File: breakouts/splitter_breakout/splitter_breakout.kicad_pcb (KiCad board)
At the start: 4 copper layers, 29.5 x 23.4 mm, 4 parts, among them U101 CONN_SMA_2GND, U102 CONN_SMA_2GND, U103 CONN_SMA_2GND, U3 PWR_SPLITTER

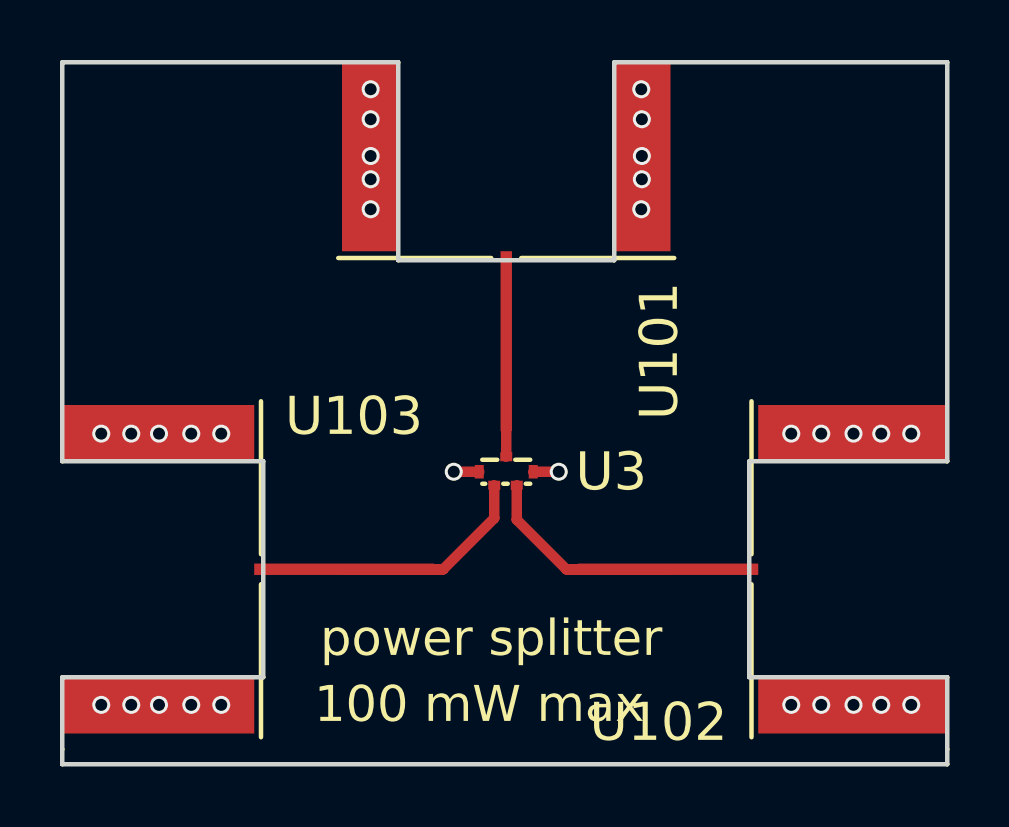
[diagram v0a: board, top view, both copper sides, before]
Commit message: modified splitter breakout to use coplanar waveguide.
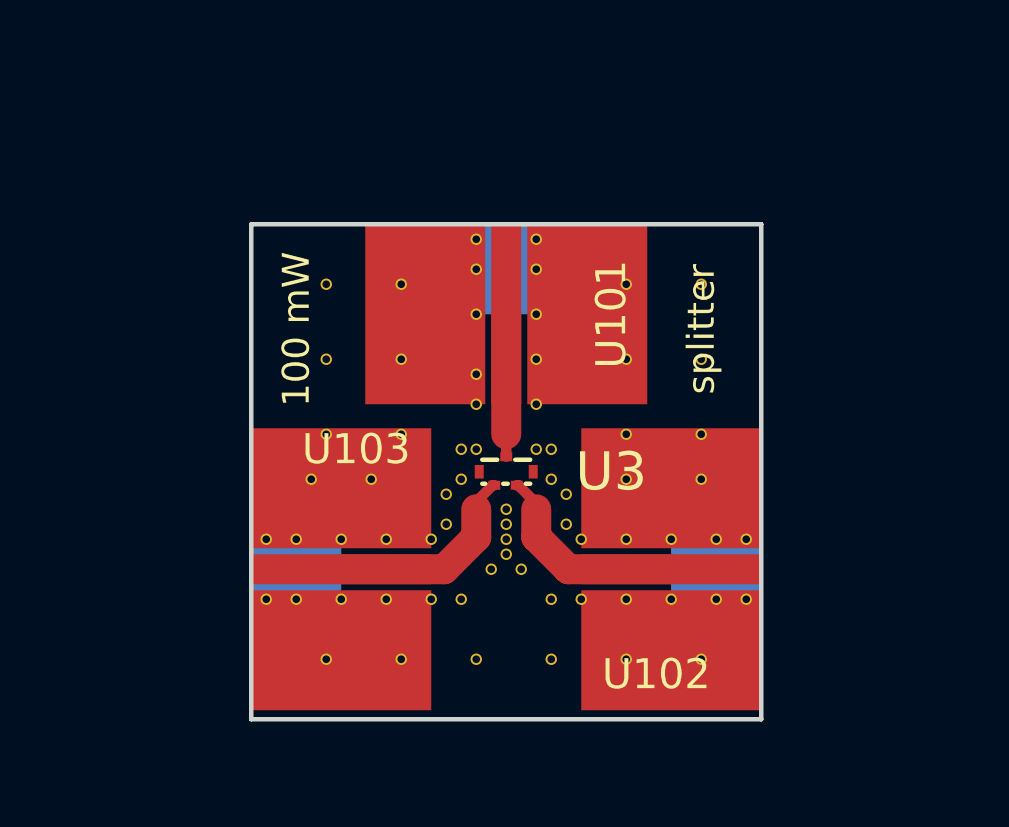
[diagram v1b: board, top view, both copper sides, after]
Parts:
- added REF**: VIA_OSH4LAYER_MIN, vna_footprints:VIA_OSH4LAYER_MIN, F.Cu at (152.5, 104.0)
- added REF**: VIA_OSH4LAYER_MIN, vna_footprints:VIA_OSH4LAYER_MIN, F.Cu at (155.0, 110.0)
- added REF**: VIA_OSH4LAYER_MIN, vna_footprints:VIA_OSH4LAYER_MIN, F.Cu at (152.5, 110.0)
- added REF**: VIA_OSH4LAYER_MIN, vna_footprints:VIA_OSH4LAYER_MIN, F.Cu at (147.5, 110.0)
- added REF**: VIA_OSH4LAYER_MIN, vna_footprints:VIA_OSH4LAYER_MIN, F.Cu at (142.5, 110.0)
- added REF**: VIA_OSH4LAYER_MIN, vna_footprints:VIA_OSH4LAYER_MIN, F.Cu at (145.0, 102.5)
- added REF**: VIA_OSH4LAYER_MIN, vna_footprints:VIA_OSH4LAYER_MIN, F.Cu at (142.5, 102.5)
- added REF**: VIA_OSH4LAYER_MIN, vna_footprints:VIA_OSH4LAYER_MIN, F.Cu at (142.5, 100.0)
- added REF**: VIA_OSH4LAYER_MIN, vna_footprints:VIA_OSH4LAYER_MIN, F.Cu at (142.5, 97.5)
- added REF**: VIA_OSH4LAYER_MIN, vna_footprints:VIA_OSH4LAYER_MIN, F.Cu at (145.0, 97.5)
- added REF**: VIA_OSH4LAYER_MIN, vna_footprints:VIA_OSH4LAYER_MIN, F.Cu at (150.0, 110.0)
- added REF**: VIA_OSH4LAYER_MIN, vna_footprints:VIA_OSH4LAYER_MIN, F.Cu at (155.0, 104.0)
- added REF**: VIA_OSH4LAYER_MIN, vna_footprints:VIA_OSH4LAYER_MIN, F.Cu at (145.0, 110.0)
- added REF**: VIA_OSH4LAYER_MIN, vna_footprints:VIA_OSH4LAYER_MIN, F.Cu at (144.0, 104.0)
- added REF**: VIA_OSH4LAYER_MIN, vna_footprints:VIA_OSH4LAYER_MIN, F.Cu at (145.0, 100.0)
- added REF**: VIA_OSH4LAYER_MIN, vna_footprints:VIA_OSH4LAYER_MIN, F.Cu at (147.5, 97.0)
- added REF**: VIA_OSH4LAYER_MIN, vna_footprints:VIA_OSH4LAYER_MIN, F.Cu at (147.5, 96.0)
- added REF**: VIA_OSH4LAYER_MIN, vna_footprints:VIA_OSH4LAYER_MIN, F.Cu at (149.5, 96.0)
- added REF**: VIA_OSH4LAYER_MIN, vna_footprints:VIA_OSH4LAYER_MIN, F.Cu at (149.5, 97.0)
- added REF**: VIA_OSH4LAYER_MIN, vna_footprints:VIA_OSH4LAYER_MIN, F.Cu at (149.5, 98.5)
- added REF**: VIA_OSH4LAYER_MIN, vna_footprints:VIA_OSH4LAYER_MIN, F.Cu at (147.5, 98.5)
- added REF**: VIA_OSH4LAYER_MIN, vna_footprints:VIA_OSH4LAYER_MIN, F.Cu at (149.5, 100.0)
- added REF**: VIA_OSH4LAYER_MIN, vna_footprints:VIA_OSH4LAYER_MIN, F.Cu at (142.0, 104.0)
- added REF**: VIA_OSH4LAYER_MIN, vna_footprints:VIA_OSH4LAYER_MIN, F.Cu at (147.5, 100.5)
- added REF**: VIA_OSH4LAYER_MIN, vna_footprints:VIA_OSH4LAYER_MIN, F.Cu at (147.5, 101.5)
- added REF**: VIA_OSH4LAYER_MIN, vna_footprints:VIA_OSH4LAYER_MIN, F.Cu at (149.5, 101.5)
- added REF**: VIA_OSH4LAYER_MIN, vna_footprints:VIA_OSH4LAYER_MIN, F.Cu at (152.5, 108.0)
- added REF**: VIA_OSH4LAYER_MIN, vna_footprints:VIA_OSH4LAYER_MIN, F.Cu at (152.5, 106.0)
- added REF**: VIA_OSH4LAYER_MIN, vna_footprints:VIA_OSH4LAYER_MIN, F.Cu at (154.0, 106.0)
- added REF**: VIA_OSH4LAYER_MIN, vna_footprints:VIA_OSH4LAYER_MIN, F.Cu at (154.0, 108.0)
- added REF**: VIA_OSH4LAYER_MIN, vna_footprints:VIA_OSH4LAYER_MIN, F.Cu at (155.5, 108.0)
- added REF**: VIA_OSH4LAYER_MIN, vna_footprints:VIA_OSH4LAYER_MIN, F.Cu at (155.5, 106.0)
- added REF**: VIA_OSH4LAYER_MIN, vna_footprints:VIA_OSH4LAYER_MIN, F.Cu at (156.5, 106.0)
- added REF**: VIA_OSH4LAYER_MIN, vna_footprints:VIA_OSH4LAYER_MIN, F.Cu at (155.0, 102.5)
- added REF**: VIA_OSH4LAYER_MIN, vna_footprints:VIA_OSH4LAYER_MIN, F.Cu at (156.5, 108.0)
- added REF**: VIA_OSH4LAYER_MIN, vna_footprints:VIA_OSH4LAYER_MIN, F.Cu at (144.5, 108.0)
- added REF**: VIA_OSH4LAYER_MIN, vna_footprints:VIA_OSH4LAYER_MIN, F.Cu at (143.0, 108.0)
- added REF**: VIA_OSH4LAYER_MIN, vna_footprints:VIA_OSH4LAYER_MIN, F.Cu at (141.5, 108.0)
- added REF**: VIA_OSH4LAYER_MIN, vna_footprints:VIA_OSH4LAYER_MIN, F.Cu at (140.5, 108.0)
- added REF**: VIA_OSH4LAYER_MIN, vna_footprints:VIA_OSH4LAYER_MIN, F.Cu at (140.5, 106.0)
- added REF**: VIA_OSH4LAYER_MIN, vna_footprints:VIA_OSH4LAYER_MIN, F.Cu at (141.5, 106.0)
- added REF**: VIA_OSH4LAYER_MIN, vna_footprints:VIA_OSH4LAYER_MIN, F.Cu at (143.0, 106.0)
- added REF**: VIA_OSH4LAYER_MIN, vna_footprints:VIA_OSH4LAYER_MIN, F.Cu at (144.5, 106.0)
- added REF**: VIA_OSH4LAYER_MIN, vna_footprints:VIA_OSH4LAYER_MIN, F.Cu at (146.0, 106.0)
- added REF**: VIA_OSH4LAYER_MIN, vna_footprints:VIA_OSH4LAYER_MIN, F.Cu at (155.0, 100.0)
- added REF**: VIA_OSH4LAYER_MIN, vna_footprints:VIA_OSH4LAYER_MIN, F.Cu at (146.5, 105.5)
- added REF**: VIA_OSH4LAYER_MIN, vna_footprints:VIA_OSH4LAYER_MIN, F.Cu at (151.0, 106.0)
- added REF**: VIA_OSH4LAYER_MIN, vna_footprints:VIA_OSH4LAYER_MIN, F.Cu at (150.5, 105.5)
- added REF**: VIA_OSH4LAYER_MIN, vna_footprints:VIA_OSH4LAYER_MIN, F.Cu at (150.5, 104.5)
- added REF**: VIA_OSH4LAYER_MIN, vna_footprints:VIA_OSH4LAYER_MIN, F.Cu at (150.0, 104.0)
- added REF**: VIA_OSH4LAYER_MIN, vna_footprints:VIA_OSH4LAYER_MIN, F.Cu at (150.0, 103.0)
- added REF**: VIA_OSH4LAYER_MIN, vna_footprints:VIA_OSH4LAYER_MIN, F.Cu at (149.5, 103.0)
- added REF**: VIA_OSH4LAYER_MIN, vna_footprints:VIA_OSH4LAYER_MIN, F.Cu at (147.5, 103.0)
- added REF**: VIA_OSH4LAYER_MIN, vna_footprints:VIA_OSH4LAYER_MIN, F.Cu at (147.0, 103.0)
- added REF**: VIA_OSH4LAYER_MIN, vna_footprints:VIA_OSH4LAYER_MIN, F.Cu at (146.5, 104.5)
- added REF**: VIA_OSH4LAYER_MIN, vna_footprints:VIA_OSH4LAYER_MIN, F.Cu at (155.0, 97.5)
- added REF**: VIA_OSH4LAYER_MIN, vna_footprints:VIA_OSH4LAYER_MIN, F.Cu at (147.0, 104.0)
- added REF**: VIA_OSH4LAYER_MIN, vna_footprints:VIA_OSH4LAYER_MIN, F.Cu at (151.0, 108.0)
- added REF**: VIA_OSH4LAYER_MIN, vna_footprints:VIA_OSH4LAYER_MIN, F.Cu at (150.0, 108.0)
- added REF**: VIA_OSH4LAYER_MIN, vna_footprints:VIA_OSH4LAYER_MIN, F.Cu at (149.0, 107.0)
- added REF**: VIA_OSH4LAYER_MIN, vna_footprints:VIA_OSH4LAYER_MIN, F.Cu at (146.0, 108.0)
- added REF**: VIA_OSH4LAYER_MIN, vna_footprints:VIA_OSH4LAYER_MIN, F.Cu at (147.0, 108.0)
- added REF**: VIA_OSH4LAYER_MIN, vna_footprints:VIA_OSH4LAYER_MIN, F.Cu at (148.0, 107.0)
- added REF**: VIA_OSH4LAYER_MIN, vna_footprints:VIA_OSH4LAYER_MIN, F.Cu at (148.5, 106.5)
- added REF**: VIA_OSH4LAYER_MIN, vna_footprints:VIA_OSH4LAYER_MIN, F.Cu at (148.5, 106.0)
- added REF**: VIA_OSH4LAYER_MIN, vna_footprints:VIA_OSH4LAYER_MIN, F.Cu at (148.5, 105.5)
- added REF**: VIA_OSH4LAYER_MIN, vna_footprints:VIA_OSH4LAYER_MIN, F.Cu at (152.5, 97.5)
- added REF**: VIA_OSH4LAYER_MIN, vna_footprints:VIA_OSH4LAYER_MIN, F.Cu at (148.5, 105.0)
- added REF**: VIA_OSH4LAYER_MIN, vna_footprints:VIA_OSH4LAYER_MIN, F.Cu at (152.5, 100.0)
- added REF**: VIA_OSH4LAYER_MIN, vna_footprints:VIA_OSH4LAYER_MIN, F.Cu at (152.5, 102.5)
- U101, U102, U103: footprint vna_footprints:142-0721-882_sma_cutout -> vna_footprints:SMA_CPW_1MM_.2MM
- moved U102 6.07 mm to (154.0, 107.0), turned to 270 degrees
- moved U103 6.07 mm to (143.0, 107.0), turned to 90 degrees
- moved U101 5.28 mm to (148.5, 98.5), turned to 0 degrees
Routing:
- net Net-(U103-Pad1): track 12.2 -> 6.95 mm
- net Net-(U102-Pad1): track 12.1 -> 6.97 mm
- net GND: track 1.70 -> 0.00 mm, vias 32 -> 0
- net Net-(U101-Pad1): track 5.75 -> 4.75 mm
- added copper zone on F.Cu, net GND
- added copper zone on In2.Cu, net GND
- removed copper zone on In1.Cu, net GND
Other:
- board size 29.5 x 23.4 mm -> 17 x 16.5 mm
- board text added: "100 mW"
- board text added: "splitter"
- board text removed: "100 mW max"
- board text removed: "power splitter"
